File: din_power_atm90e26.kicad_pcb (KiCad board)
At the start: 2 copper layers, 86.9 x 32.8 mm, 62 parts, among them J1 CONN_01X06, J2 VBAT, J3 CONN_01X08, J4 CONN_02X18, J5 CONN_01X08, U1 MCP73831-2-OT, U2 AP7365-33YG-13, U3 AP7365-33YG-13, U4 Hi-Link_SMPS, U5 dc-dc

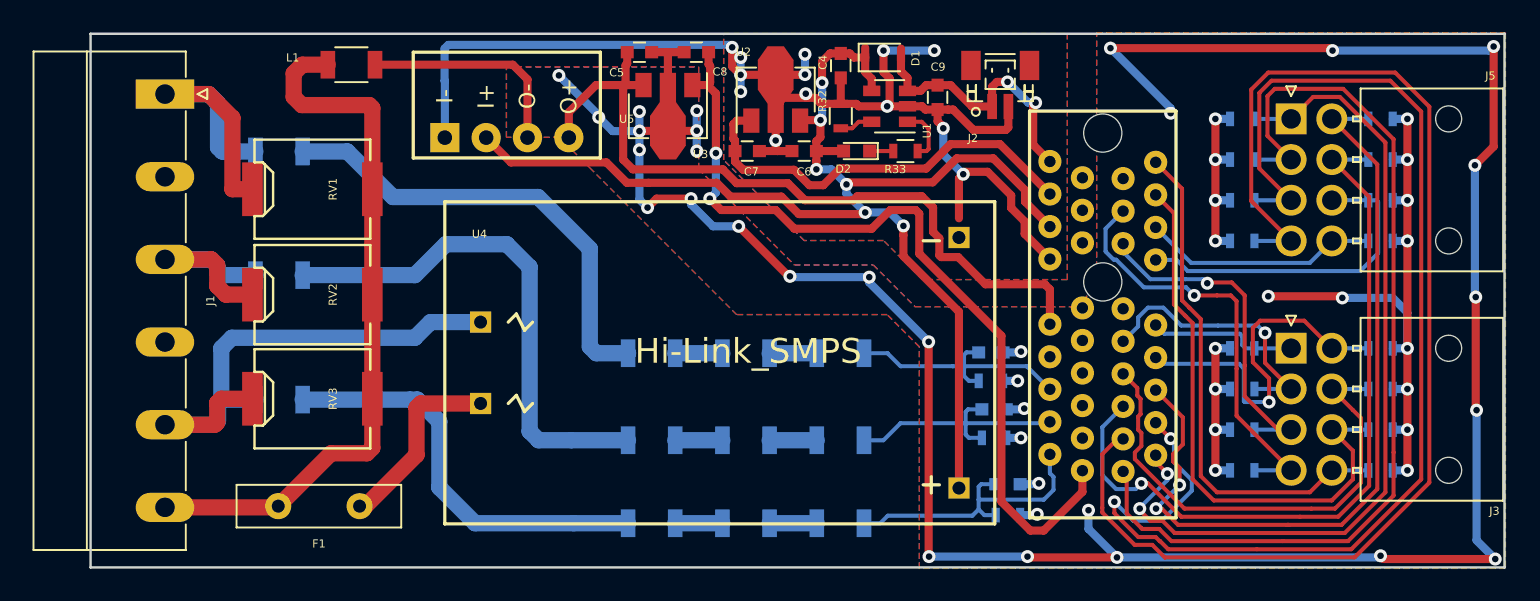
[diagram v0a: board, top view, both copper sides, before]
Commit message: Updates links to new KiCAD libraries
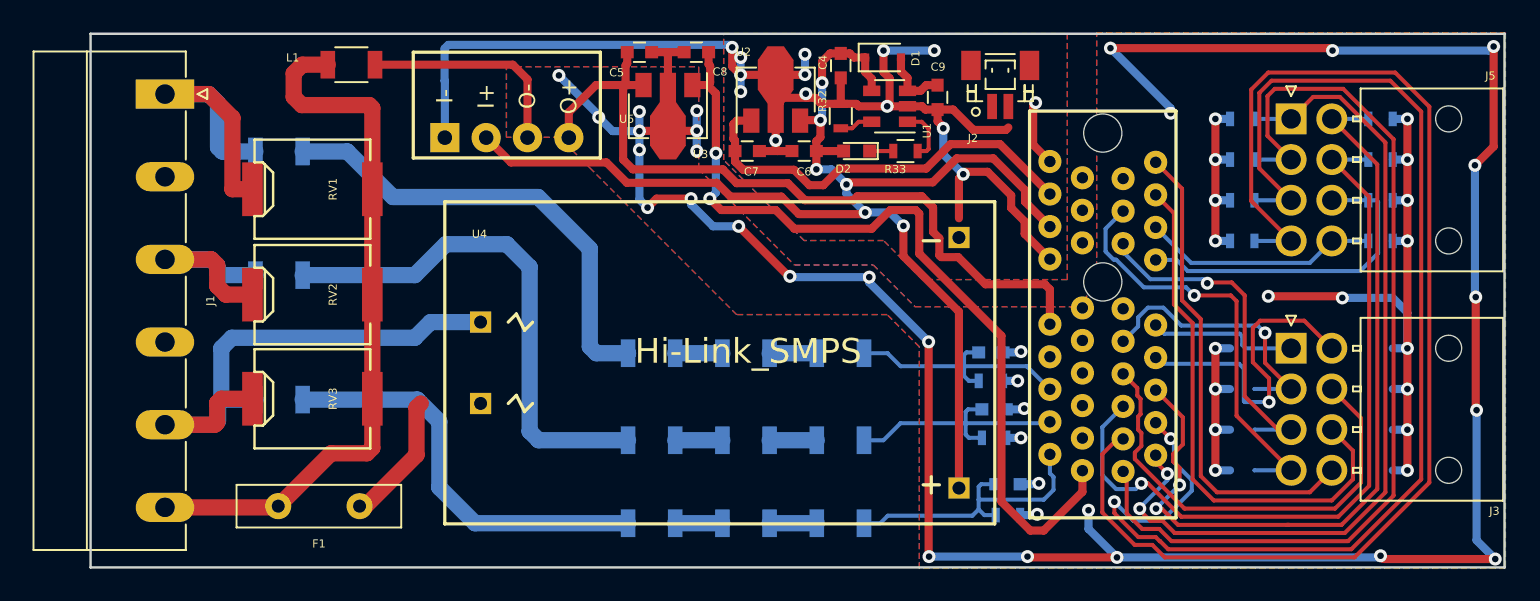
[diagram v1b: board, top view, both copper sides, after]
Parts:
- removed R18, R19, R20, R21, R28, R29, R30, R31: 5.8R, Resistors_SMD:R_0603
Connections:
- J2 pad 1: VBAT -> Net-(J2-Pad1)
- J2 pad 2: GNDPWR -> Net-(J2-Pad2)
- U4 pad 2: /UN_IN -> Net-(U4-Pad2)
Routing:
- net VBAT: track 17.3 -> 8.32 mm, vias 2 -> 1
- net /UN_IN: track 11.8 -> 8.07 mm
- net IC2+: track 22.2 -> 20.0 mm
- net IN2+: track 35.2 -> 32.9 mm
- net IC2-: track 30.6 -> 28.3 mm
- net IN2-: track 31.7 -> 29.5 mm
- net GNDPWR: track 78.1 -> 76.8 mm
- net +5V: track 80.7 -> 80.1 mm

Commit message: Ripped out routing and added individual optos
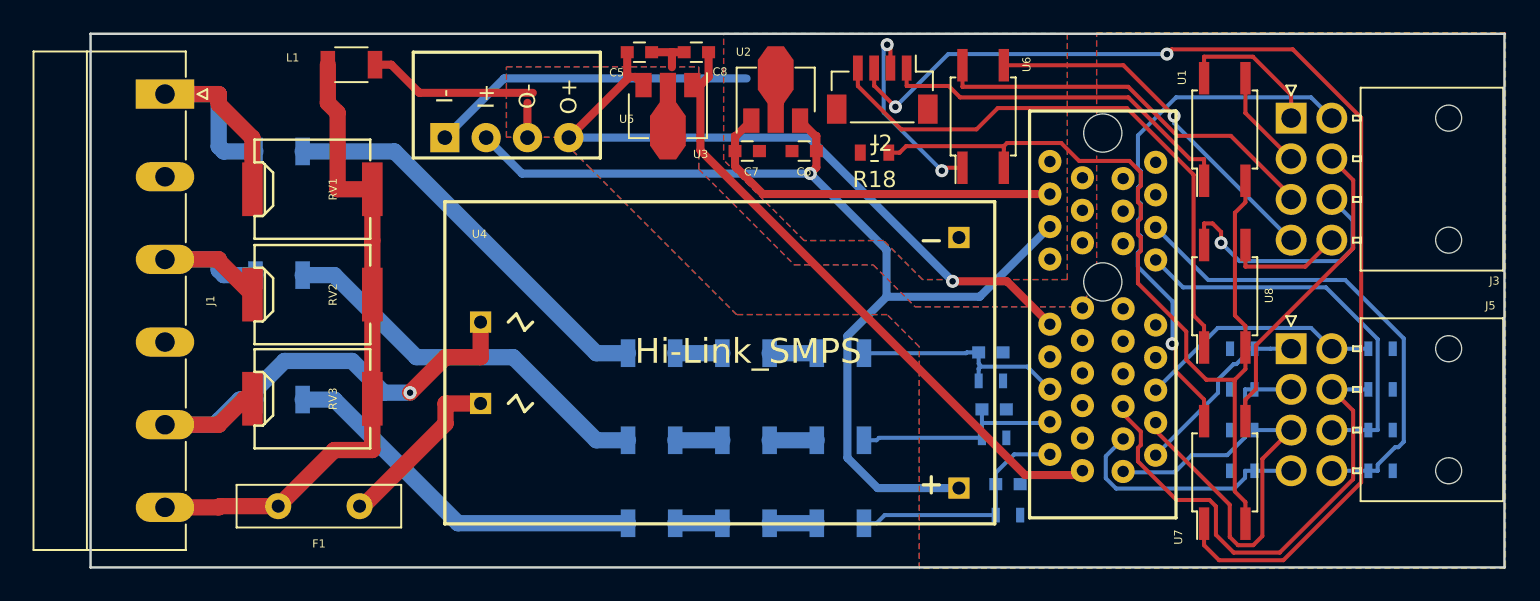
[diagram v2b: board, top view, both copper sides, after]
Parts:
- removed C4, C9: 1uF, Capacitors_SMD:C_0603
- removed D1: D_Schottky, Diodes_SMD:D_SOD-323F
- removed D2: LED, LEDs:LED_0603
- removed R32: 2K, Resistors_SMD:R_0603
- removed R33: 1K, Resistors_SMD:R_0603
- added R18: R, Resistor_SMD:R_0603_1608Metric, F.Cu at (154.1, 52.8)
- added U6: LTV-356T, Package_SO:SO-4_4.4x3.6mm_P2.54mm, F.Cu at (160.8, 50.5)
- added U7: LTV-356T, Package_SO:SO-4_4.4x3.6mm_P2.54mm, F.Cu at (175.6, 72.4)
- added U8: LTV-356T, Package_SO:SO-4_4.4x3.6mm_P2.54mm, F.Cu at (175.6, 61.6)
- J2: value VBAT -> Conn_01x04; footprint Connectors_JST:JST_SH_BM02B-SRSS-TB_02x1.00mm_Straight -> Connector_JST:JST_SH_BM04B-SRSS-TB_1x04-1MP_P1.00mm_Vertical
- U1: value MCP73831-2-OT -> LTV-356T; footprint TO_SOT_Packages_SMD:SOT-23-5 -> Package_SO:SO-4_4.4x3.6mm_P2.54mm
- U2: value AP7365-33YG-13 -> L78L33_SOT89
- U3: value AP7365-33YG-13 -> L78L05_SOT89
- moved U1 20.6 mm to (175.6, 51.4), turned to 90 degrees
- moved J3 14.1 mm to (179.7, 50.6)
- moved J5 14.1 mm to (179.7, 64.8)
- moved R1 14.1 mm to (176.7, 64.8)
- moved R10 14.1 mm to (185.2, 69.8)
- moved R11 14.1 mm to (185.2, 72.3)
- moved R2 14.1 mm to (176.7, 67.3)
- moved R3 14.1 mm to (185.2, 64.8)
- moved R4 14.1 mm to (185.2, 67.3)
- moved R8 14.1 mm to (176.7, 69.8)
- moved R9 14.1 mm to (176.7, 72.3)
- moved J2 7.25 mm to (154.6, 48.9), turned to 180 degrees
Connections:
- J2 pad 1: Net-(J2-Pad1) -> LED_H1
- J2 pad 2: Net-(J2-Pad2) -> LED_H2
- J3 pad 1: IA2+ -> RE1_H
- J3 pad 2: IA2- -> RE1_L
- J3 pad 3: IB2+ -> RE2_H
- J3 pad 4: IB2- -> RE2_L
- J3 pad 5: IC2+ -> RE3_H
- J3 pad 6: IC2- -> RE3_L
- J3 pad 7: IN2+ -> RE4_H
- J3 pad 8: IN2- -> RE4_L
- U1 pad 1: Net-(R33-Pad2) -> LED_H1
- U1 pad 2: GNDPWR -> LED_L
- U1 pad 3: VBAT -> RE1_L
- U1 pad 4: +5V -> RE1_H
- U4 pad 2: Net-(U4-Pad2) -> /UN_IN
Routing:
- net GNDA: track 239.7 -> 15.5 mm, vias 51 -> 0
- net LED_H3: track 0.00 -> 70.5 mm, vias 0 -> 2
- net IB1-: track 76.8 -> 15.2 mm
- net GNDPWR: track 76.8 -> 20.1 mm, vias 13 -> 0
- net LED_L: track 0.00 -> 56.6 mm
- net IB1+: track 76.9 -> 20.9 mm, vias 2 -> 0
- net IA1-: track 59.7 -> 14.2 mm
- net IA1+: track 52.5 -> 11.7 mm, vias 2 -> 0
- net LED_H4: track 0.00 -> 36.0 mm
- net IC1+: track 50.2 -> 15.2 mm, vias 2 -> 0
- net RE3_H: track 0.00 -> 33.1 mm, vias 0 -> 1
- net IN2+: track 32.9 -> 0.00 mm
- net IN2-: track 29.5 -> 0.00 mm
- net IC2-: track 28.3 -> 0.00 mm
- net IB2-: track 26.3 -> 0.00 mm, vias 1 -> 0
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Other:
- board text added: "Whatnick Emon Relay v0.1 25/04/2019"
- board text removed: "Whatnick Emon Base v1.2 07/12/2017"

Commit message: Added routing for Opto-driver based PCB
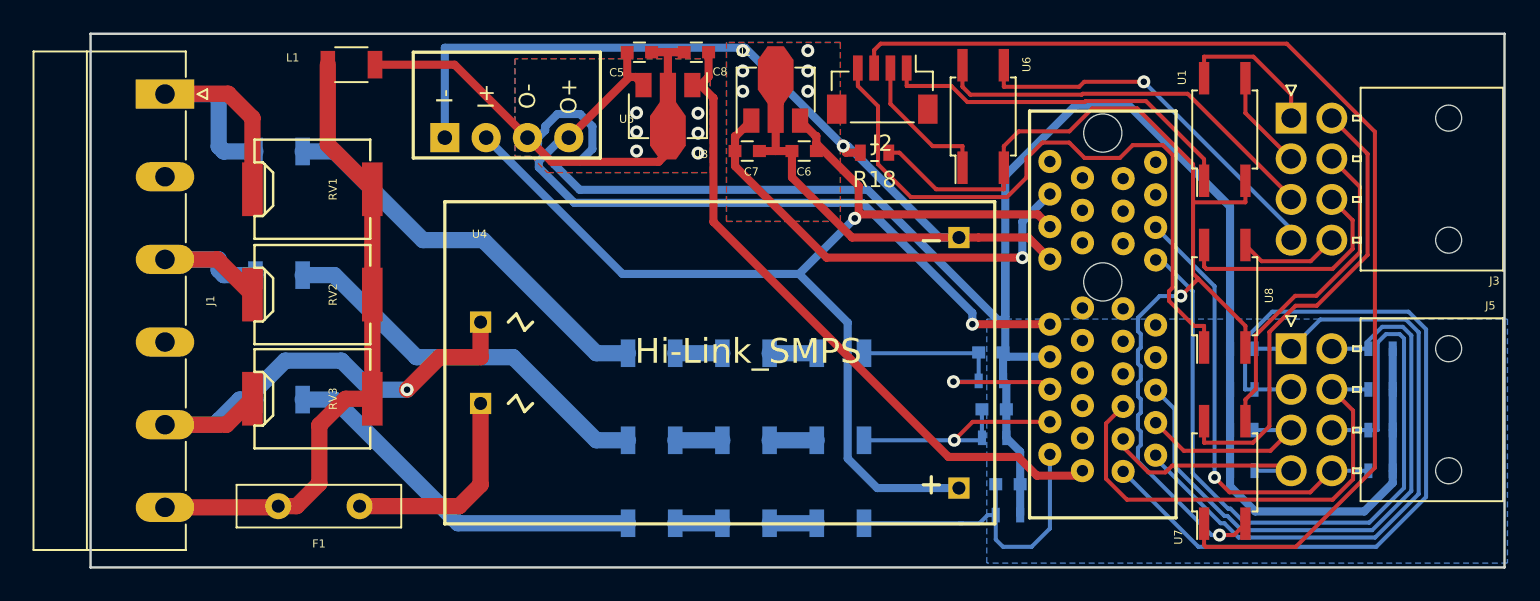
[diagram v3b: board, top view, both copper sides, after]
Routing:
- net GNDA: track 15.5 -> 153.6 mm, vias 0 -> 6
- net GNDPWR: track 20.1 -> 70.9 mm, vias 0 -> 7
- net IA1-: track 14.2 -> 50.3 mm
- net IA1+: track 11.7 -> 40.6 mm
- net IN1+: track 24.1 -> 48.7 mm
- net IC1+: track 15.2 -> 37.9 mm
- net IB1+: track 20.9 -> 11.8 mm
- net LED_L: track 56.6 -> 64.7 mm, vias 0 -> 2
- net UC_SAMP: track 14.7 -> 20.4 mm
- net LED_H4: track 36.0 -> 41.6 mm
- net +3V3: track 23.3 -> 27.8 mm, vias 0 -> 1
- net +5V_ISO: track 42.2 -> 46.6 mm
- net RE3_H: track 33.1 -> 28.9 mm, vias 1 -> 0
- net +5V: track 64.5 -> 67.9 mm
- net LED_H2: track 12.2 -> 9.03 mm, vias 2 -> 0
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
